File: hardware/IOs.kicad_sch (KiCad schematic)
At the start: 20 parts

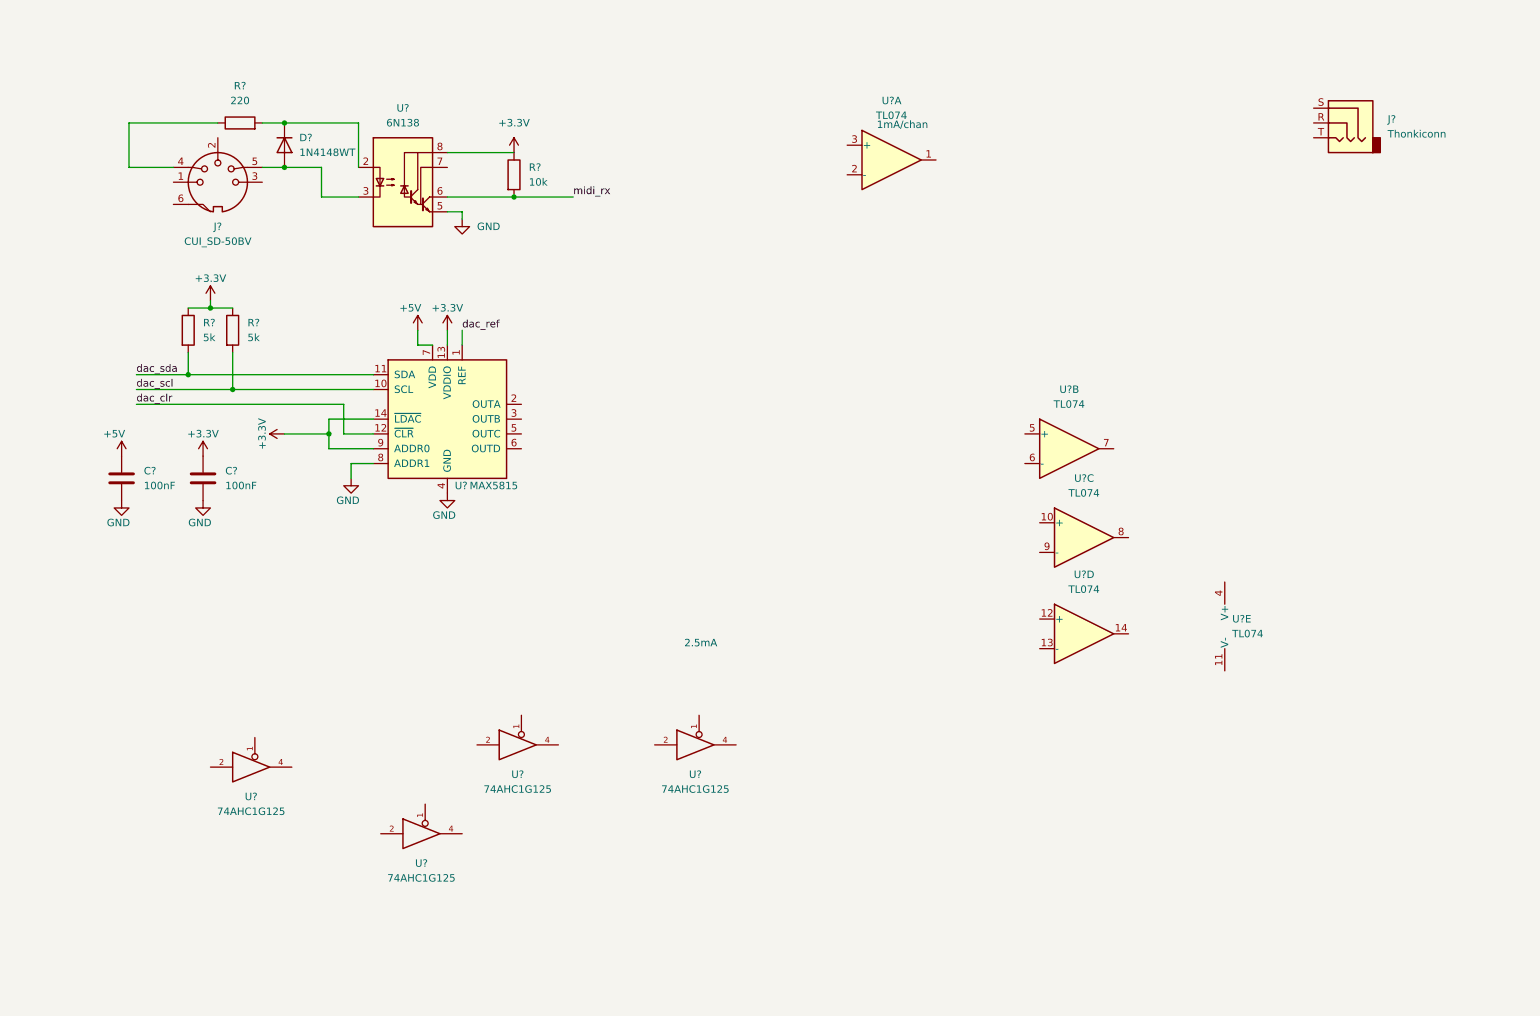
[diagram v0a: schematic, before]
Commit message: MAX5715BAUD lib added
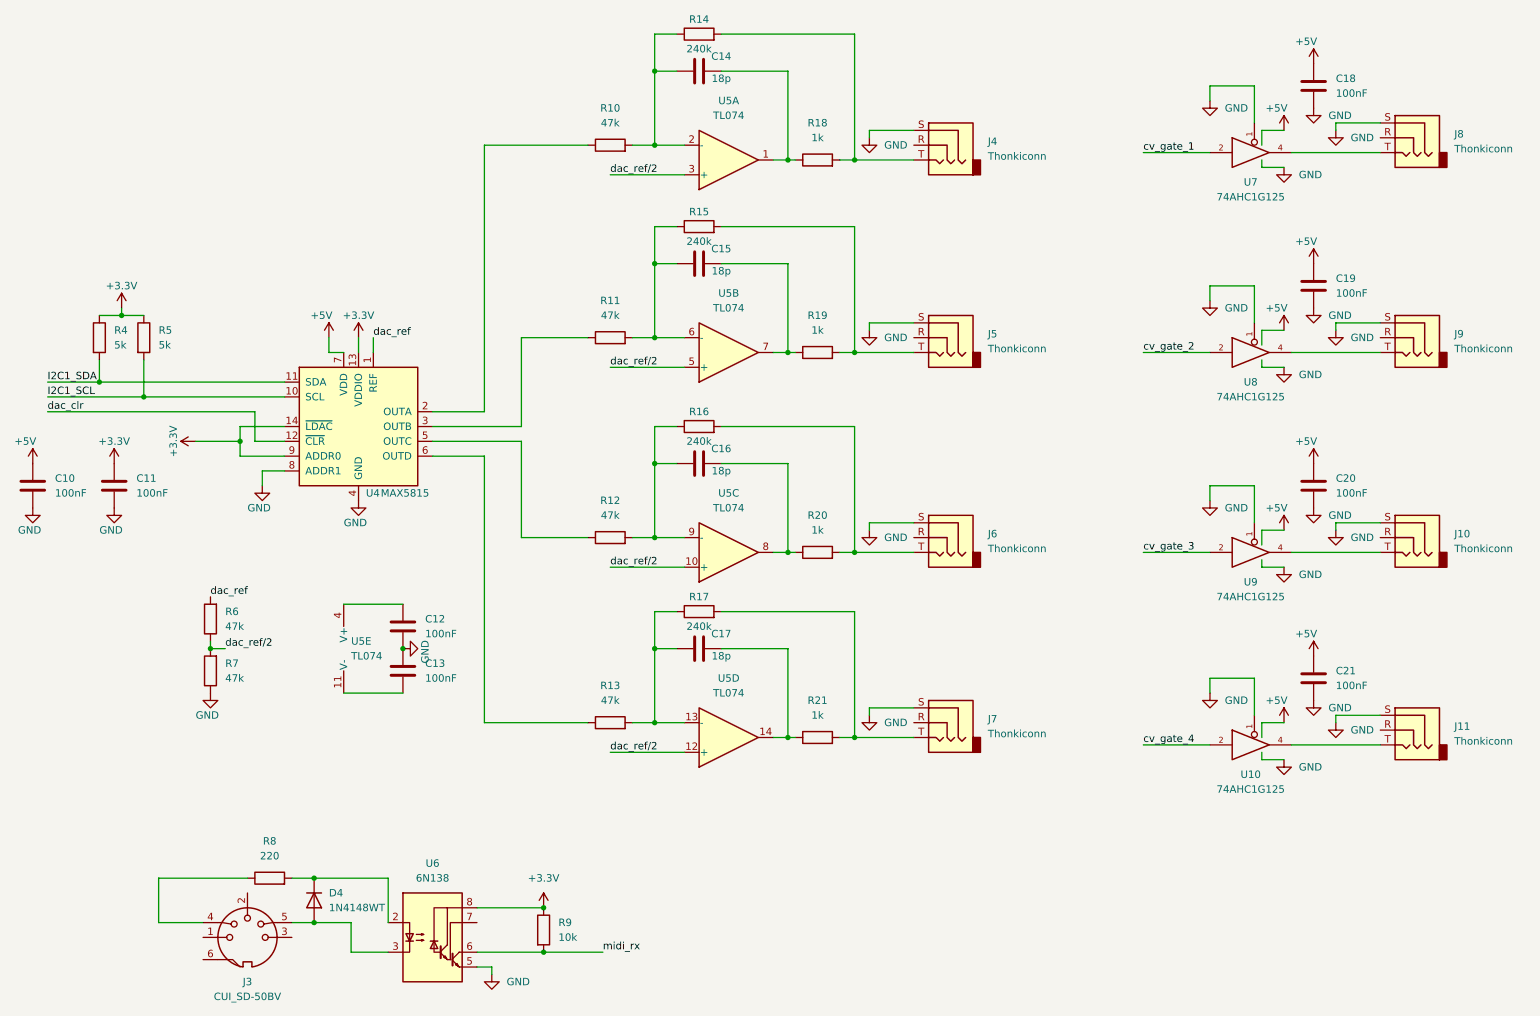
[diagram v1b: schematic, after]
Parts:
- removed U? (x3): 74AHC1G125, Package_TO_SOT_SMD:SOT-23-5, symbol 74xGxx:74AHC1G125
- added C12, C13, C18, C19, C20, C21: 100nF, Capacitor_SMD:C_0603_1608Metric, symbol Device:C
- added C14, C15, C16, C17: 18p, Capacitor_SMD:C_0603_1608Metric, symbol Device:C
- added J10, J11, J5, J6, J7, J8, J9: Thonkiconn, Connector_Audio:Jack_3.5mm_QingPu_WQP-PJ398SM_Vertical_CircularHoles, symbol Connector:AudioJack3
- added R10, R11, R12, R13, R6, R7: 47k, Resistor_SMD:R_0603_1608Metric, symbol Device:R
- added R14, R15, R16, R17: 240k, Resistor_SMD:R_0603_1608Metric, symbol Device:R
- added R18, R19, R20, R21: 1k, Resistor_SMD:R_0603_1608Metric, symbol Device:R
- added U10, U8, U9: 74AHC1G125, Package_TO_SOT_SMD:SOT-23-5, symbol 74xGxx:74AHC1G125
- gave numbers to parts that had none: 13
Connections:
- net VCC is gone; now on net +5V: U7.5 (VCC)
- net +5V: now also C18.1, C19.1, C20.1, C21.1, U10.5 (VCC), U8.5 (VCC), U9.5 (VCC)
- net GND: now also J4.S, U7.1, C12.2, C13.1, C18.2, C19.2, C20.2, C21.2, J10.S, J11.S, J5.S, J6.S, J7.S, J8.S, J9.S, R7.1, U10.1, U10.3 (GND), U8.1, U8.3 (GND), U9.1, U9.3 (GND)
- net dac_ref: now also R6.2
- net dac_ref/2: now reaches U5.10 (+)
- net dac_ref/2: now also U5.12 (+), U5.3 (+), U5.5 (+), R6.1, R7.2
- net at U5.8: now also C16.2, R20.1
- net at U5.9 (-): now also C16.1, R12.2, R16.1
- net at U4.2 (OUTA): now also R10.1
- net at U4.3 (OUTB): now also R11.1
- net at U4.5 (OUTC): now also R12.1
- net at U4.6 (OUTD): now also R13.1
- net at U5.6 (-): now also C15.1, R11.2, R15.1
- net at U5.7: now also C15.2, R19.1
- net at U5.11 (V-): now also C13.2
- net at U5.4 (V+): now also C12.1
- net at U5.13 (-): now also C17.1, R13.2, R17.1
- net at U5.14: now also C17.2, R21.1
- net at J4.T: now also R14.2, R18.2
- net cv_gate_1: now reaches U7.2
- net at U7.4: now also J8.T
- net at U5.1: now also C14.2, R18.1
- net at U5.2 (-): now also C14.1, R10.2, R14.1
- net dac_scl renamed I2C1_SCL
- net dac_sda renamed I2C1_SDA
- new net: J6.T, R16.2, R20.2
- new net: J7.T, R17.2, R21.2
- new net: J5.T, R15.2, R19.2
- new net: J9.T, U8.4
- new net: J10.T, U9.4
- new net: J11.T, U10.4
- new net cv_gate_2: U8.2
- new net cv_gate_3: U9.2
- new net cv_gate_4: U10.2
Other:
- note removed: "1mA/chan"
- note removed: "2.5mA"
- moved on the sheet: C10, C11, D4, J3, J4, R4, R5, R8, R9, U4, U5A, U5B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

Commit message: chore: resync local state
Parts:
- removed C18, C19, C20, C21: 100nF, Capacitor_SMD:C_0603_1608Metric, symbol Device:C
- removed D4: 1N4148WT, Diode_SMD:D_SOD-523, symbol Diode:1N4148WT
- removed J10, J11, J8, J9: Thonkiconn, Connector_Audio:Jack_3.5mm_QingPu_WQP-PJ398SM_Vertical_CircularHoles, symbol Connector:AudioJack3
- removed J3: CUI_SD-50BV, midi_euro_lib:CUI_SD-50BV, symbol midi_euro_lib:CUI_SD-50BV
- removed R8: 220, Resistor_SMD:R_0805_2012Metric, symbol Device:R
- removed R9: 10k, Resistor_SMD:R_0603_1608Metric, symbol Device:R
- removed U10, U7, U8, U9: 74AHC1G125, Package_TO_SOT_SMD:SOT-23-5, symbol 74xGxx:74AHC1G125
- removed U6: 6N138, Package_DIP:SMDIP-8_W9.53mm, symbol Isolator:6N138
